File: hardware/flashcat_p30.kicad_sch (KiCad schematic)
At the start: 15 parts, among them J1 EC56 J1 (control/data), J2 EC56 J2 (address), U1 PC28F256P30T85, U2 TLV75518PDBV

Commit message: feat(hardware): wire balls B8/H1 to header A26/A27 for Micron P30-65nm 1/2 Gbit parts
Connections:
- net A26: now reaches U1.B8 (A26)
- net A26: now also J2.3 (A26/RB2)
- net A27: now reaches U1.H1 (A27)
- net A27: now also J2.1 (A27/RB1)
- no-connect marks 15 -> 11
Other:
- note added: "NOTES 1. Ball names follow the P30 datasheet (row letter A-H along the 13 mm side, column number 1-8). Pads of the socket footprint carry the same names; mapping remapped from the S29 footprint supplied by Embedded Computers. 2. x16 WORD addressing: FlashcatUSB drives header A1..A27 in x16 mode, so P30 A1 (LSB) -> header A1. Header A0 is unused. A25 is used by 512 Mbit parts; B8 = A26 (1 Gbit) an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"
- note removed: "NOTES 1. Ball names follow the P30 datasheet (row letter A-H along the 13 mm side, column number 1-8). Pads of the socket footprint carry the same names; mapping remapped from the S29 footprint supplied by Embedded Computers. 2. x16 WORD addressing: FlashcatUSB drives header A1..A27 in x16 mode, so P30 A1 (LSB) -> header A1. Header A0 is unused. A25 is only used by 512 Mbit (dual-die) parts, A26/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"
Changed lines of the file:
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@@
 		)
 	)
-	(no_connect
-		(at 215.9 182.88)
+	(wire
+		(pts
+			(xy 198.12 175.26) (xy 193.04 175.26)
+		)
+		(stroke
+			(width 0)
+			(type default)
+		)
+	)
+	(label "A26"
+		(at 193.04 175.26 180)
+		(effects
+			(font
+				(size 1.27 1.27)
+			)
+			(justify right bottom)
+		)
 	)
 	(wire
@@
 	)
 	(no_connect
-		(at 218.44 182.88)
+		(at 215.9 182.88)
 	)
 	(no_connect
-		(at 220.98 182.88)
+		(at 218.44 182.88)
 	)
 	(wire
@@
 	)
 	(no_connect
-		(at 223.52 182.88)
+		(at 220.98 182.88)
 	)
 	(wire
@@
 		)
 	)
-	(no_connect
-		(at 226.06 182.88)
+	(wire
+		(pts
+			(xy 198.12 177.8) (xy 193.04 177.8)
+		)
+		(stroke
+			(width 0)
+			(type default)
+		)
+	)
+	(label "A27"
+		(at 193.04 177.8 180)
+		(effects
+			(font
+				(size 1.27 1.27)
+			)
+			(justify right bottom)
+		)
 	)
 	(wire
@@
 		)
 	)
-	(no_connect
-		(at 111.76 163.83)
+	(wire
+		(pts
+			(xy 111.76 163.83) (xy 116.84 163.83)
+		)
+		(stroke
+			(width 0)
+			(type default)
+		)
+	)
+	(label "A27"
+		(at 116.84 163.83 0)
+		(effects
+			(font
+				(size 1.27 1.27)
+			)
+			(justify left bottom)
+		)
 	)
 	(no_connect
 		(at 86.36 163.83)
 	)
-	(no_connect
-		(at 111.76 166.37)
+	(wire
+		(pts
+			(xy 111.76 166.37) (xy 116.84 166.37)
+		)
+		(stroke
+			(width 0)
+			(type default)
+		)
+	)
+	(label "A26"
+		(at 116.84 166.37 0)
+		(effects
+			(font
+				(size 1.27 1.27)
+			)
+			(justify left bottom)
+		)
 	)
 	(wire
@@
 		)
 	)
-	(text "NOTES\n1. Ball names follow the P30 datasheet (row letter A-H along the 13 mm side, column number 1-8).\n   Pads of the socket footprint carry the same names; mapping remapped from the S29 footprint\n   supplied by Embedded Computers.\n2. x16 WORD addressing: FlashcatUSB drives header A1..A27 in x16 mode, so P30 A1 (LSB) -> header A1.\n   Header A0 is unused. A25 is only used by 512 Mbit (dual-die) parts, A26/A27 are unused.\n3. P30 VCC (core) is 1.7-2.0 V, ABS MAX 2.5 V. U2 makes 1.8 V from the programmer VCC:\n   programmer at 3.3 V -> regulated 1.8 V; programmer at 1.8 V -> U2 in dropout, ~1.78 V.\n   VCCQ (I/O, 1.7-3.6 V) is fed from header VCC, header VIO is unused (same as the EC P30\n   TSOP-56 Type-D adapter). VPP (VPPL 0.9-3.6 V) is tied to header VCC; U2 feeds VCC only.\n4. ADV# and CLK tied to GND (asynchronous mode). WAIT -> header RB0 with 4.7k pull-up. RFU open.\n5. RST#, WP# are not on the EC header. WP# is tied to header VCC (lock-down off, as the EC\n   TSOP-56 Type-D adapter); RST# is pulled up to header VCC with a ~1 ms power-on delay.\n   CE#, OE#, WE# are driven directly by the programmer (no pull-ups, as the EC adapters).\n6. Unused EC header pins (VPP, VIO, CLE, ALE, RE/B#, DQS, A0, A26, A27) are left open."
+	(text "NOTES\n1. Ball names follow the P30 datasheet (row letter A-H along the 13 mm side, column number 1-8).\n   Pads of the socket footprint carry the same names; mapping remapped from the S29 footprint\n   supplied by Embedded Computers.\n2. x16 WORD addressing: FlashcatUSB drives header A1..A27 in x16 mode, so P30 A1 (LSB) -> header A1.\n   Header A0 is unused. A25 is used by 512 Mbit parts; B8 = A26 (1 Gbit) and H1 = A27 (2 Gbit)\n   only exist on Micron P30-65nm (RFU on 130 nm parts), wired as EC's TSOP-56 Type-D does.\n3. P30 VCC (core) is 1.7-2.0 V, ABS MAX 2.5 V. U2 makes 1.8 V from the programmer VCC:\n   programmer at 3.3 V -> regulated 1.8 V; programmer at 1.8 V -> U2 in dropout, ~1.78 V.\n   VCCQ (I/O, 1.7-3.6 V) is fed from header VCC, header VIO is unused (same as the EC P30\n   TSOP-56 Type-D adapter). VPP (VPPL 0.9-3.6 V) is tied to header VCC; U2 feeds VCC only.\n4. ADV# and CLK tied to GND (asynchronous mode). WAIT -> header RB0 with 4.7k pull-up. RFU open.\n5. RST#, WP# are not on the EC header. WP# is tied to header VCC (lock-down off, as the EC\n   TSOP-56 Type-D adapter); RST# is pulled up to header VCC with a ~1 ms power-on delay.\n   CE#, OE#, WE# are driven directly by the programmer (no pull-ups, as the EC adapters).\n6. Unused EC header pins (VPP, VIO, CLE, ALE, RE/B#, DQS, A0) are left open."
 		(exclude_from_sim no)
 		(at 25.4 228.6 0)

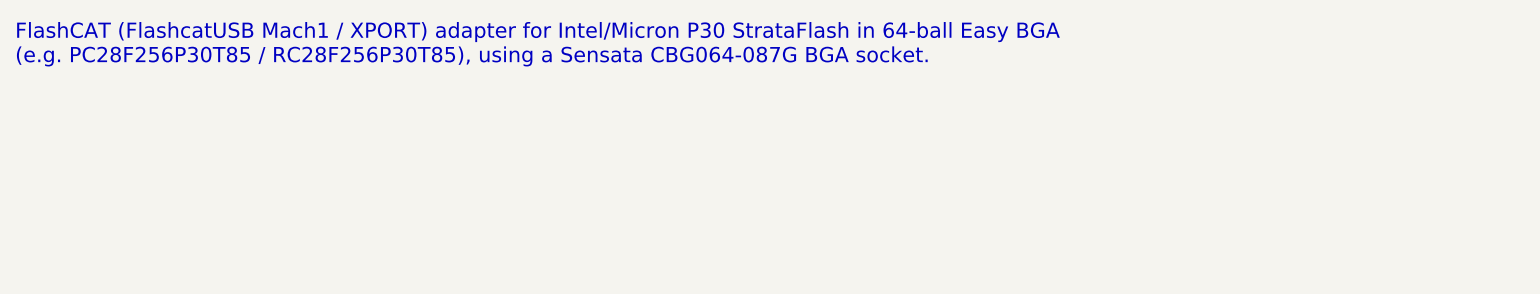
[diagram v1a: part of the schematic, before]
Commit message: feat(hardware): switch to the HMILU BGA64-1.0-TP21NS 10x13 mm socket on a 51x33 mm board
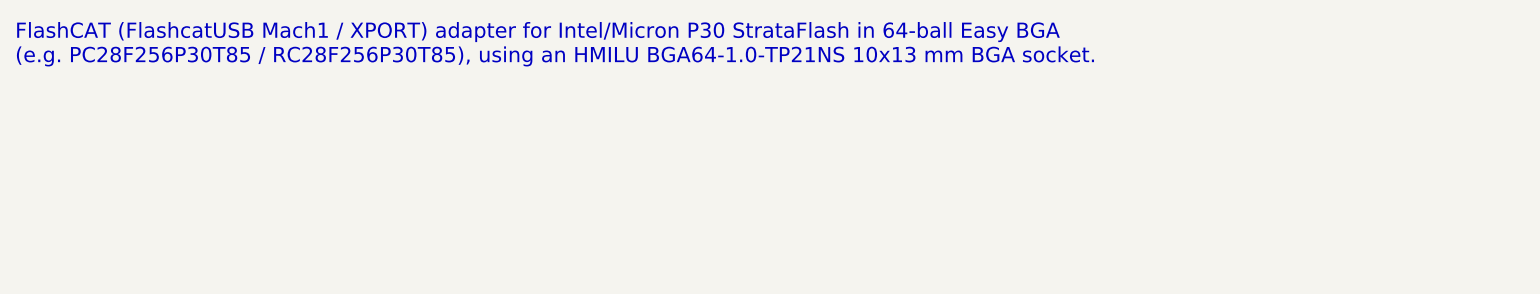
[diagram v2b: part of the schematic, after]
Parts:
- U1: footprint flashcat_p30:Sensata_CBG064-087G -> flashcat_p30:HMILU_BGA64-1.0-TP21NS; MPN CBG064-087G -> BGA64-1.0-TP21NS; Manufacturer Sensata Technologies -> HMILU; Socket Sensata CBG064-087G -> HMILU BGA64-1.0-TP21NS
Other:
- note added: "FlashCAT (FlashcatUSB Mach1 / XPORT) adapter for Intel/Micron P30 StrataFlash in 64-ball Easy BGA (e.g. PC28F256P30T85 / RC28F256P30T85), using an HMILU BGA64-1.0-TP21NS 10x13 mm BGA socket."
- note removed: "FlashCAT (FlashcatUSB Mach1 / XPORT) adapter for Intel/Micron P30 StrataFlash in 64-ball Easy BGA (e.g. PC28F256P30T85 / RC28F256P30T85), using a Sensata CBG064-087G BGA socket."
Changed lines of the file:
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@@
 	(title_block
 		(title "FlashCAT P30 Easy BGA-64 adapter")
-		(date "2026-09-27")
-		(rev "B")
+		(date "2026-10-02")
+		(rev "C")
 		(company "brainstorm@nopcode.org")
-		(comment 1 "Socket: Sensata CBG064-087G. Target: Intel/Micron StrataFlash P30 (Easy BGA-64)")
+		(comment 1 "Socket: HMILU BGA64-1.0-TP21NS. Target: Intel/Micron StrataFlash P30 (Easy BGA-64)")
 		(comment 2 "Plugs into the Embedded Computers 56-pin dual header (FlashcatUSB Mach1 / XPORT)")
 	)
@@
 			)
 		)
-		(property "Footprint" "flashcat_p30:Sensata_CBG064-087G"
+		(property "Footprint" "flashcat_p30:HMILU_BGA64-1.0-TP21NS"
 			(at 215.9 142.24 0)
 			(hide yes)
@@
 			)
 		)
-		(property "Description" "Intel/Micron StrataFlash P30 parallel NOR, 64-ball Easy BGA (10x13 mm, 1.0 mm pitch), fitted in a Sensata CBG064-087G burn-in socket"
+		(property "Description" "Intel/Micron StrataFlash P30 parallel NOR, 64-ball Easy BGA (10x13 mm, 1.0 mm pitch), fitted in an HMILU BGA64-1.0-TP21NS socket"
 			(at 215.9 142.24 0)
 			(hide yes)
@@
 			)
 		)
-		(property "Socket" "Sensata CBG064-087G"
+		(property "Socket" "HMILU BGA64-1.0-TP21NS"
 			(at 215.9 142.24 0)
 			(hide yes)
@@
 			)
 		)
-		(property "MPN" "CBG064-087G"
+		(property "MPN" "BGA64-1.0-TP21NS"
 			(at 215.9 142.24 0)
 			(hide yes)
@@
 			)
 		)
-		(property "Manufacturer" "Sensata Technologies"
+		(property "Manufacturer" "HMILU"
 			(at 215.9 142.24 0)
 			(hide yes)
@@
 		)
 	)
-	(text "FlashCAT (FlashcatUSB Mach1 / XPORT) adapter for Intel/Micron P30 StrataFlash in 64-ball Easy BGA\n(e.g. PC28F256P30T85 / RC28F256P30T85), using a Sensata CBG064-087G BGA socket."
+	(text "FlashCAT (FlashcatUSB Mach1 / XPORT) adapter for Intel/Micron P30 StrataFlash in 64-ball Easy BGA\n(e.g. PC28F256P30T85 / RC28F256P30T85), using an HMILU BGA64-1.0-TP21NS 10x13 mm BGA socket."
 		(exclude_from_sim no)
 		(at 25.4 22.86 0)
